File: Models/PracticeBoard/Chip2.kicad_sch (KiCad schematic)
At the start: 17 parts, among them U1 XMC1100

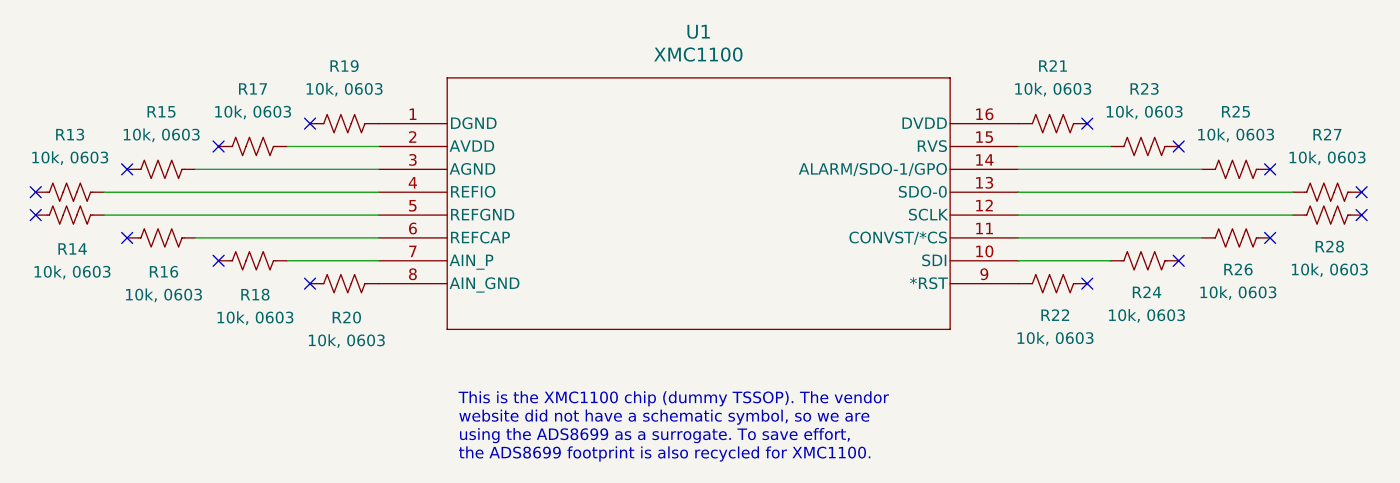
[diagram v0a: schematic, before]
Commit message: Finished the schematic for the practice board
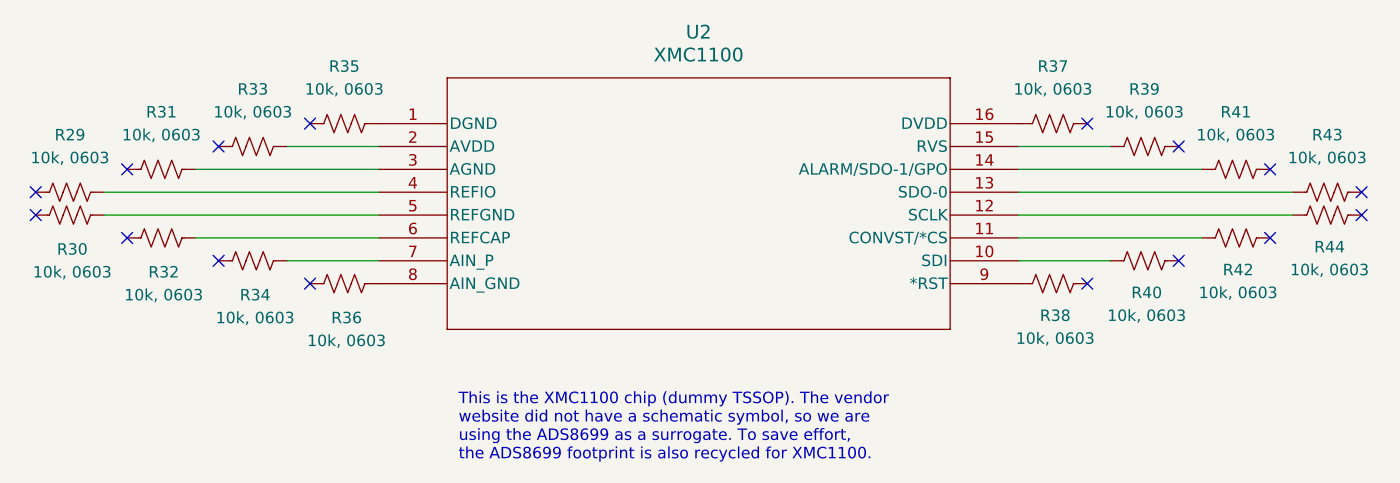
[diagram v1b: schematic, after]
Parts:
- removed R13, R14, R15, R16, R17, R18, R19, R20, R21, R22, R23, R24, R25, R26, R27, R28: 10k, 0603, TwoTerminal:RESC0603, symbol Device:R_US
- removed U1: XMC1100, IC:ADS8699, symbol ADS8699:ADS8699IPW
- added R29, R30, R31, R32, R33, R34, R35, R36, R37, R38, R39, R40, R41, R42, R43, R44: 10k, 0603, TwoTerminal:RESC0603, symbol Device:R_US
- added U2: XMC1100, IC:ADS8699, symbol ADS8699:ADS8699IPW
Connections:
- new net: R37.1, U2.16 (DVDD)
- new net: R31.2, U2.3 (AGND)
- new net: R40.1, U2.10 (SDI)
- new net: R44.1, U2.12 (SCLK)
- new net: R43.1, U2.13 (SDO-0)
- new net: R36.2, U2.8 (AIN_GND)
- new net: R33.2, U2.2 (AVDD)
- new net: R35.2, U2.1 (DGND)
- new net: R30.2, U2.5 (REFGND)
- new net: R41.1, U2.14 (ALARM/SDO-1/GPO)
- new net: R39.1, U2.15 (RVS)
- new net: R32.2, U2.6 (REFCAP)
- new net: R38.1, U2.9 (*RST)
- new net: R42.1, U2.11 (CONVST/*CS)
- new net: R29.2, U2.4 (REFIO)
- new net: R34.2, U2.7 (AIN_P)
